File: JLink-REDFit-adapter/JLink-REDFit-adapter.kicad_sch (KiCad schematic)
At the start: 8 parts, among them J1 UART_ClientSide, J2 2x10 female header 2.54mm pit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, J3 Jitter_Debug_HostSide, J4 Conn_01x06_Socket

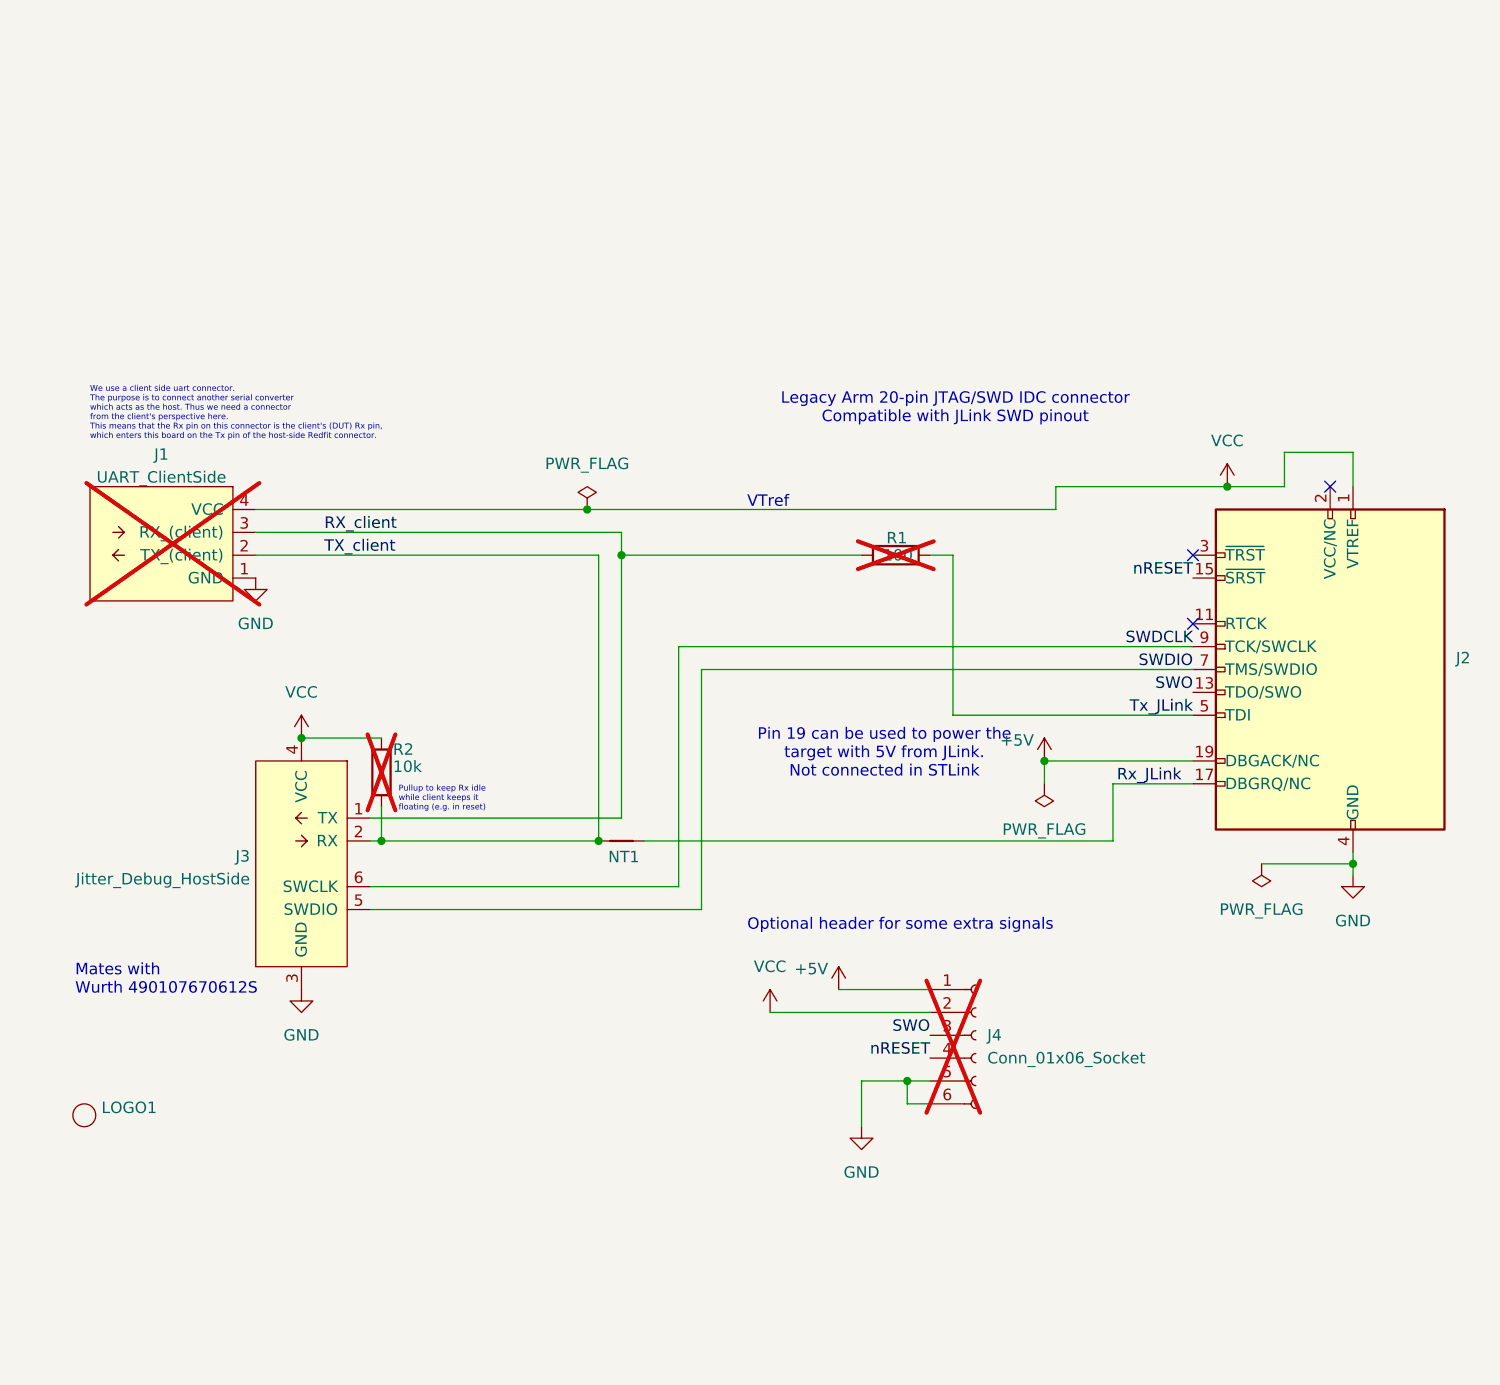
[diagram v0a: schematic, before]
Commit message: Modernize the adapter boards
This repo contains adapter boards for the Jitter 6-pins REDFit debug
interface to multiple standard programming/debug tools.
Each now renamed to make this clearer (BMP/HSProbe/JLink) and save those
projects as modern Kicad10 designs
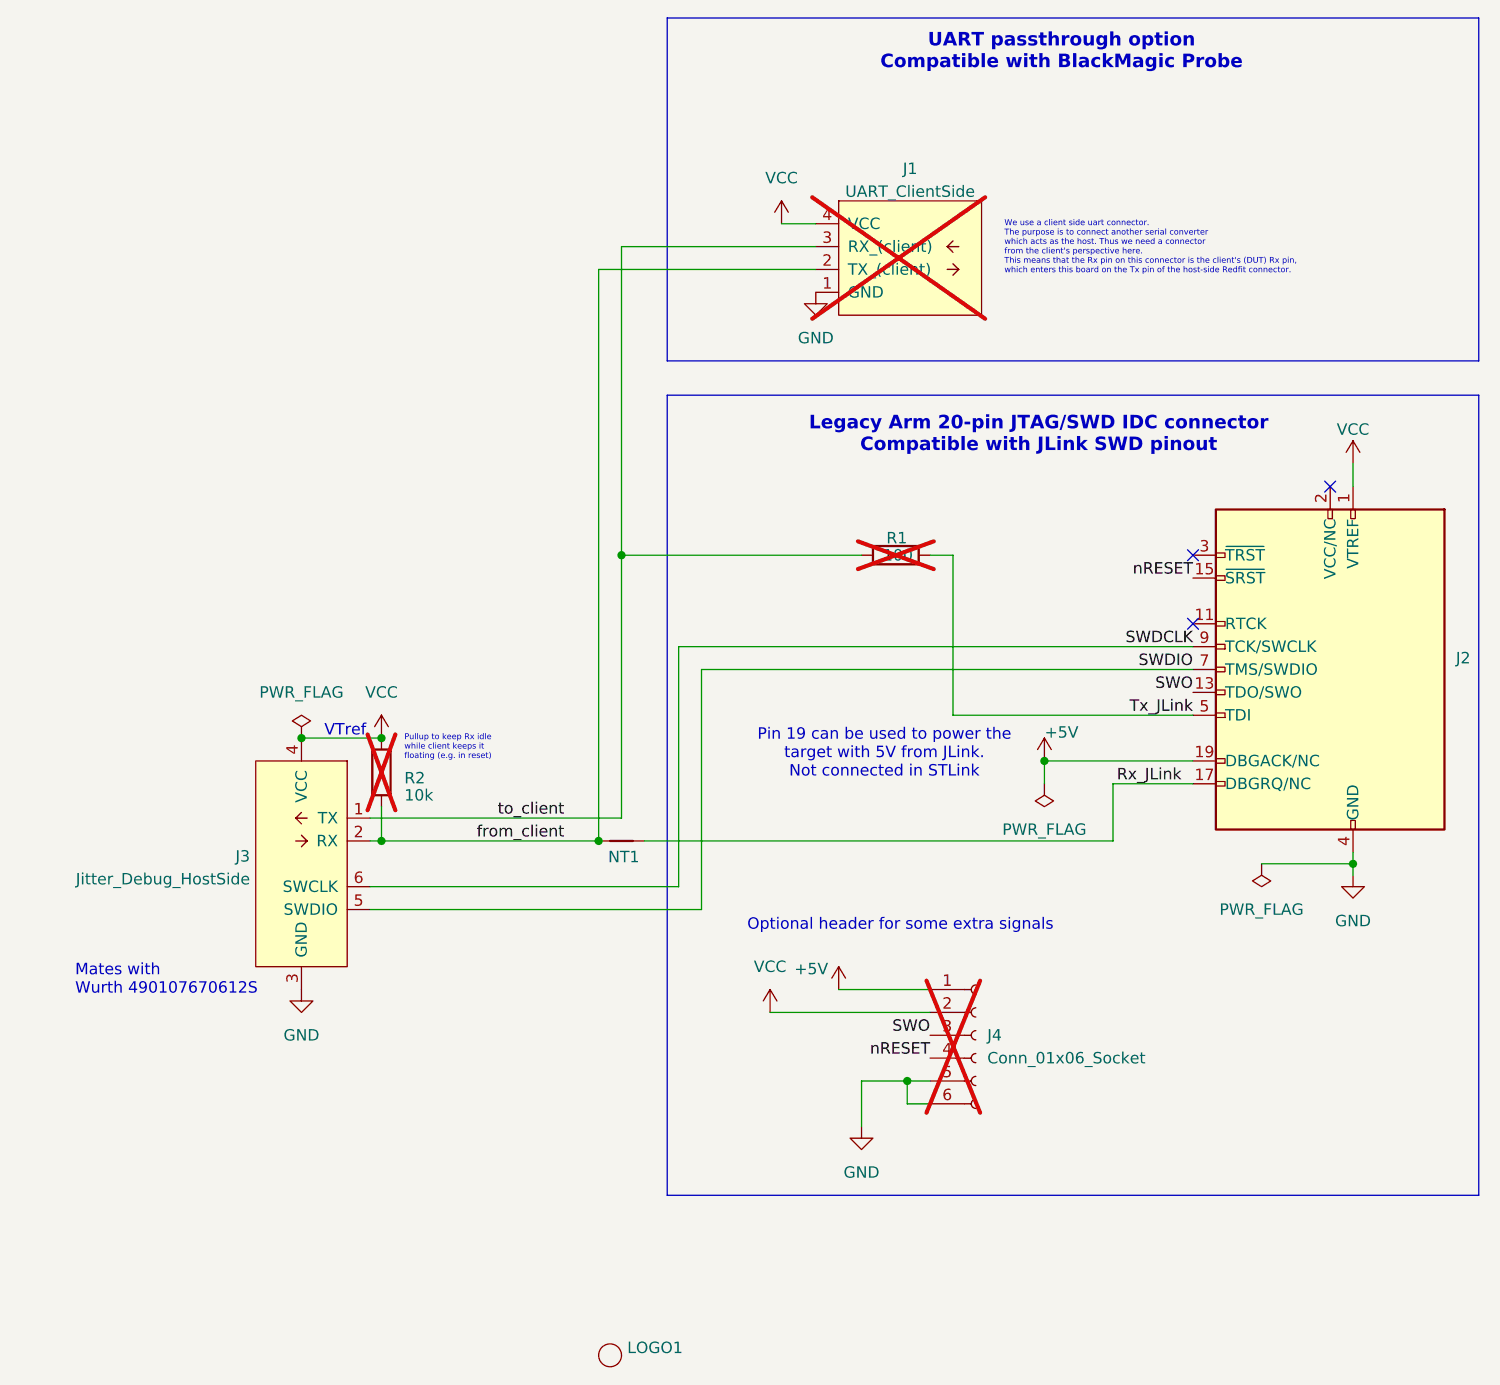
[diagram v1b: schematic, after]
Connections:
- net RX_client renamed to_client
- net TX_client renamed from_client
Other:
- note added: "UART passthrough option Compatible with BlackMagic Probe"
- title: JLink - REDfit adapter -> JLink-REDfit adapter
- moved on the sheet: J1, LOGO1
